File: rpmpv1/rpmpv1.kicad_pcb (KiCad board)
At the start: 2 copper layers, 102.7 x 65.3 mm, 7 parts, among them J1 RPi_GPIO, P1 CONN_02X25, U1 74LS245, U2 74LS245, U3 74LS245, U4 74LS245, U5 74LS245

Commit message: update board for RPMP
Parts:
- added REF**: 1pin, Connectors:1pin, F.Cu at (128.5, 58.3)
- added REF**: 1pin, Connectors:1pin, F.Cu at (186.5, 58.3)
- U2: moved to B.Cu
- U4, U5: moved to F.Cu
- moved J1 49.9 mm to (181.6, 59.6), turned to 90 degrees
- moved U1 20.5 mm to (175.5, 80.0), turned to 270 degrees
- moved U4 20.4 mm to (157.8, 80.0), turned to 270 degrees
- moved U3 20.3 mm to (139.4, 80.0)
- moved U5 8.92 mm to (140.7, 80.0)
- moved U2 4.47 mm to (157.8, 80.0), turned to 270 degrees
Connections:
- U1 pad 16: /INT -> /BUSDIR
- U1 pad 17: /WAIT -> /INT
- U1 pad 18: /BUSDIR -> /WAIT
- U1 pad 2: /RBUSDIR -> /RWAIT
- U1 pad 3: /RWAIT -> /RINT
- U1 pad 4: /RINT -> /RBUSDIR
- U4 pad 11: Net-(U4-Pad11) -> /RESET
- U4 pad 12: Net-(U4-Pad12) -> /WR
- U4 pad 13: /SLTSL -> /RD
- U4 pad 14: /MREQ -> /IORQ
- U4 pad 15: /IORQ -> /MREQ
- U4 pad 16: /RD -> /SLTSL
- U4 pad 17: /WR -> Net-(U4-Pad17)
- U4 pad 18: /RESET -> Net-(U4-Pad18)
- U4 pad 2: /RA13 -> Net-(U4-Pad2)
- U4 pad 3: /RA14 -> Net-(U4-Pad3)
- U4 pad 4: /RA8 -> /RA11
- U4 pad 5: /RA12 -> /RA10
- U4 pad 6: /RA10 -> /RA12
- U4 pad 7: /RA11 -> /RA8
- U4 pad 8: Net-(U4-Pad8) -> /RA14
- U4 pad 9: Net-(U4-Pad9) -> /RA13
- U5 pad 11: /A1 -> /A6
- U5 pad 12: /A0 -> /A7
- U5 pad 13: /A3 -> /A4
- U5 pad 14: /A2 -> /A5
- U5 pad 15: /A5 -> /A2
- U5 pad 16: /A4 -> /A3
- U5 pad 17: /A7 -> /A0
- U5 pad 18: /A6 -> /A1
- U5 pad 2: /RD6 -> /RD1
- U5 pad 3: /RD7 -> /RD0
- U5 pad 4: /RD4 -> /RD3
- U5 pad 5: /RD5 -> /RD2
- U5 pad 6: /RD2 -> /RD5
- U5 pad 7: /RD3 -> /RD4
- U5 pad 8: /RD0 -> /RD7
- U5 pad 9: /RD1 -> /RD6
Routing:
- net +5V: track 0.00 -> 149.6 mm, vias 0 -> 1
- net GND: track 0.00 -> 142.3 mm, vias 0 -> 13
- net /RCLK: track 0.00 -> 92.5 mm
- net /CLK: track 0.00 -> 80.2 mm, vias 0 -> 2
- net /RD4: track 0.00 -> 73.5 mm, vias 0 -> 1
- net /RWAIT: track 0.00 -> 66.4 mm
- net /RINT: track 0.00 -> 65.9 mm, vias 0 -> 1
- net /RD: track 0.00 -> 59.7 mm, vias 0 -> 1
- net /RD2: track 0.00 -> 57.1 mm, vias 0 -> 2
- net /LE_A: track 0.00 -> 56.6 mm
- net /LE_B: track 0.00 -> 53.8 mm, vias 0 -> 1
- net /RD3: track 0.00 -> 52.7 mm, vias 0 -> 1
- net /SLTSL: track 0.00 -> 52.6 mm
- net /A6: track 0.00 -> 47.7 mm, vias 0 -> 2
- net /A7: track 0.00 -> 47.3 mm, vias 0 -> 1
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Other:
- board size 102.7 x 65.3 mm -> 65.1 x 64.4 mm

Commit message: update for rpmcv1 and rpspc
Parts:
- U1: value 74LS245 -> 74LS05; footprint Housings_SOIC:SOIC-20W_7.5x12.8mm_Pitch1.27mm -> Housings_SOIC:SOIC-14_3.9x8.7mm_Pitch1.27mm
- moved U1 0.75 mm to (175.0, 79.4), turned to 90 degrees
- renumbered REF** to REF1
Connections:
- U1 pad 1: GND -> /RWAIT
- U1 pad 10: GND -> (no net)
- U1 pad 11: Net-(U1-Pad11) -> (no net)
- U1 pad 12: Net-(U1-Pad12) -> (no net)
- U1 pad 13: Net-(U1-Pad13) -> (no net)
- U1 pad 14: Net-(U1-Pad14) -> +5V
- U1 pad 2: /RWAIT -> /WAIT
- U1 pad 4: /RBUSDIR -> /INT
- U1 pad 5: /CLK -> /RBUSDIR
- U1 pad 6: Net-(U1-Pad6) -> /BUSDIR
- U1 pad 7: Net-(U1-Pad7) -> GND
- U1 pad 8: Net-(U1-Pad8) -> /RCLK
- U1 pad 9: Net-(U1-Pad9) -> /CLK
- U2 pad 1: +5V -> GND
- U3 pad 1: /RD -> /WR
- U4 pad 1: +5V -> GND
- U5 pad 1: +5V -> GND
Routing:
- net GND: track 142.3 -> 0.00 mm, vias 13 -> 0
- net /RCLK: track 92.5 -> 56.6 mm
- net +5V: track 149.6 -> 120.6 mm, vias 1 -> 3
- net /RD: track 59.7 -> 32.6 mm, vias 1 -> 0
- net /WR: track 33.3 -> 58.6 mm, vias 1 -> 2
- net /RA8: track 22.5 -> 45.0 mm, vias 1 -> 0
- net /RWAIT: track 66.4 -> 44.8 mm
- net /RD1: track 42.4 -> 23.6 mm, vias 0 -> 1
- net /RA10: track 19.5 -> 36.8 mm, vias 1 -> 0
- net /RD5: track 37.0 -> 21.0 mm, vias 0 -> 1
- net /RD6: track 38.1 -> 23.5 mm, vias 0 -> 1
- net /RINT: track 65.9 -> 51.7 mm, vias 1 -> 0
- net /RA12: track 38.4 -> 25.9 mm
- net /RD0: track 36.0 -> 23.7 mm, vias 0 -> 1
- net /RA13: track 34.2 -> 22.6 mm
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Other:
- outline, holes or cut-outs redrawn

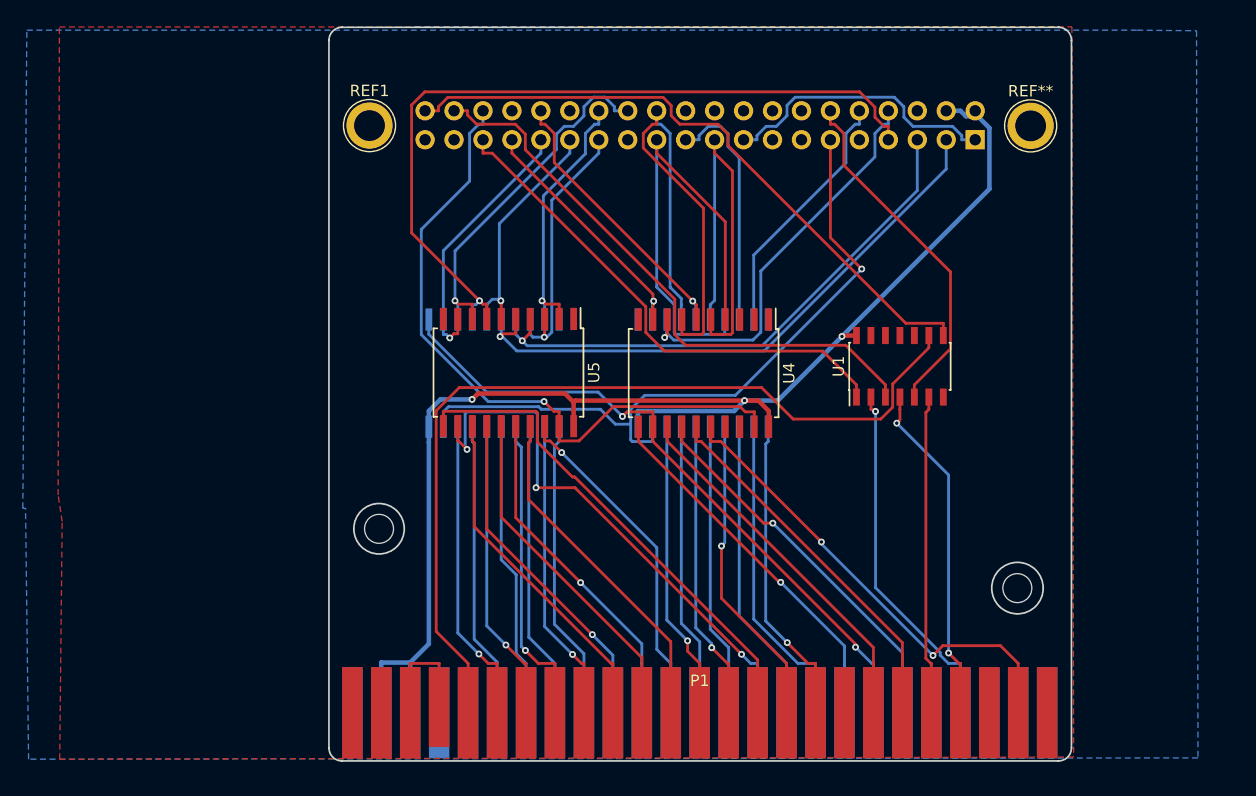
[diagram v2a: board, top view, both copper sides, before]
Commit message: improvement for RPMP feature
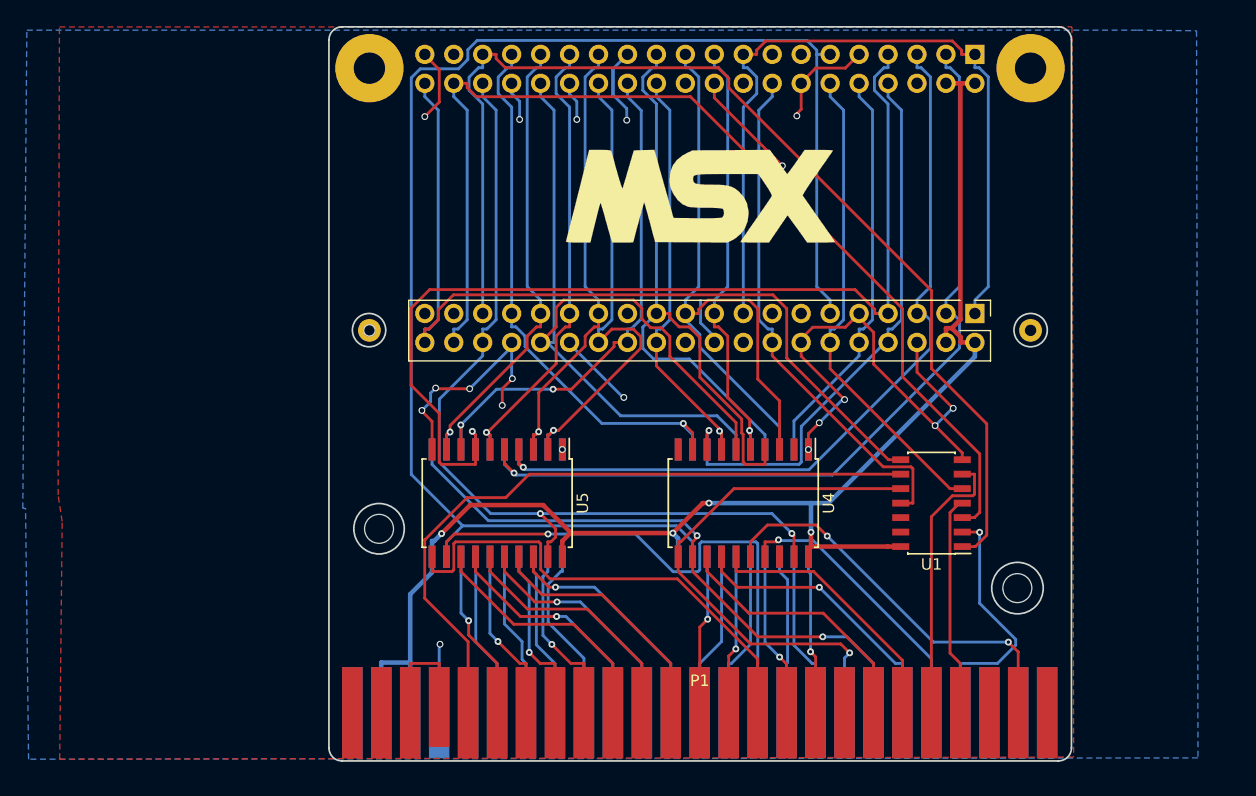
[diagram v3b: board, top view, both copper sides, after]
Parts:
- removed the REF** at (186.5, 58.3)
- removed REF1: 1pin, Connectors:1pin
- added G***: LOGO, MSX:msx-logo, F.Cu at (157.5, 64.5)
- added J2: RPi_GPIO, Socket_Strips:Socket_Strip_Straight_2x20_Pitch2.54mm, B.Cu at (181.6, 52.1)
- added REF**: Raspberry_Pi_Zero, MSX:Raspberry_Pi_Zero_Layout, F.Cu at (190.0, 49.8)
- J1: footprint Pin_Headers:Pin_Header_Straight_2x20_Pitch2.54mm -> Socket_Strips:Socket_Strip_Straight_2x20_Pitch2.54mm
- moved J1 15.2 mm to (181.6, 74.8)
- moved U1 12.3 mm to (177.8, 91.4), turned to 180 degrees
- moved U2 11.9 mm to (161.3, 91.4)
- moved U4 11.9 mm to (161.3, 91.4)
- moved U5 11.5 mm to (139.7, 91.4)
- moved U3 11.4 mm to (139.7, 91.4)
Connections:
- J1 pad 16: Net-(J1-Pad16) -> /RRESET
- P1 pad 9: Net-(P1-Pad9) -> /M1
- U1 pad 10: (no net) -> /RESET
- U1 pad 11: (no net) -> /RRESET
- U4 pad 17: Net-(U4-Pad17) -> /M1
- U4 pad 3: Net-(U4-Pad3) -> /RA9
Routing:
- net GND: track 0.00 -> 124.0 mm, vias 0 -> 19
- net /LE_B: track 62.3 -> 129.1 mm, vias 1 -> 0
- net /RWAIT: track 44.8 -> 98.6 mm
- net /RA12: track 25.9 -> 73.7 mm, vias 1 -> 0
- net /RRESET: track 0.00 -> 45.6 mm
- net +3V3: track 24.9 -> 69.6 mm
- net /RINT: track 51.7 -> 94.1 mm
- net /RA9: track 21.4 -> 59.8 mm
- net /RA13: track 22.6 -> 49.5 mm
- net /M1: track 0.00 -> 25.0 mm, vias 0 -> 1
- net /RD2: track 53.1 -> 76.7 mm
- net /RD3: track 49.3 -> 71.9 mm
- net /RA11: track 41.6 -> 63.3 mm
- net /RD4: track 69.0 -> 90.1 mm
- net /RCLK: track 56.6 -> 77.1 mm
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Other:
- outline, holes or cut-outs redrawn

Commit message: minor update for rpspc, rpmcv4, rpmpv1
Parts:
- removed the REF** at (190.0, 49.8)
- added C1: 33n, Capacitors_SMD:C_0805_HandSoldering, B.Cu at (129.5, 63.5)
- added C2: 10u, Capacitors_SMD:C_0805_HandSoldering, B.Cu at (129.5, 66.0)
- added R1: 270R, Resistors_SMD:R_0805_HandSoldering, B.Cu at (129.5, 61.0)
- added R2: 150R, Resistors_SMD:R_0805_HandSoldering, B.Cu at (129.5, 68.6)
- added REF**: Raspberry_Pi_Zero, 8BIT:Raspberry_Pi_Zero_Layout, F.Cu at (125.0, 79.7)
- moved J1 0.14 mm to (181.7, 74.9)
- moved J2 0.14 mm to (181.7, 51.9)
- renumbered P1 to ?
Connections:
- ? pad 49: Net-(P1-Pad49) -> /SOUNDIN
- J1 pad 12: /RBUSDIR -> /BCK
- J1 pad 15: Net-(J1-Pad15) -> /RBUSDIR
- J1 pad 18: Net-(J1-Pad18) -> /RWAIT
- J1 pad 22: Net-(J1-Pad22) -> /RCLK
- J1 pad 35: /RWAIT -> /LRCK
- J1 pad 40: /RCLK -> /DOUT
- J2 pad 12: /RBUSDIR -> /BCK
- J2 pad 15: Net-(J2-Pad15) -> /RBUSDIR
- J2 pad 18: Net-(J2-Pad18) -> /RWAIT
- J2 pad 22: Net-(J2-Pad22) -> /RCLK
- J2 pad 35: /RWAIT -> /LRCK
- J2 pad 40: /RCLK -> /DOUT
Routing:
- net /SOUNDIN: track 0.00 -> 45.7 mm
- net /LRCK: track 0.00 -> 38.4 mm
- net /RWAIT: track 98.6 -> 62.4 mm
- net /RCLK: track 77.1 -> 49.8 mm
- net /RA12: track 73.7 -> 49.7 mm, vias 0 -> 1
- net /DOUT: track 0.00 -> 24.0 mm
- net /BCK: track 0.00 -> 24.0 mm
- net /RA11: track 63.3 -> 42.2 mm, vias 0 -> 1
- net /RA8: track 37.4 -> 55.9 mm, vias 1 -> 0
- net /RD6: track 41.2 -> 59.6 mm, vias 1 -> 0
- net /RD4: track 90.1 -> 108.0 mm
- net /RINT: track 94.1 -> 76.6 mm
- net /RA9: track 59.8 -> 42.8 mm, vias 0 -> 1
- net /RBUSDIR: track 42.2 -> 50.5 mm
- net /A7: track 47.6 -> 39.3 mm
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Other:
- board text added: "2018.01.19"
- board text added: "5V"
- board text added: "74LS05"
- board text added: "74LS245"
- board text added: "ADDRESS"
- board text added: "BD"
- board text added: "CLK"
- board text added: "CS12"
- board text added: "DATA"
- board text added: "GND"
- board text added: "INT"
- board text added: "IQ"
- board text added: "M1"
- board text added: "MQ"
- board text added: "RD"
- board text added: "RST"
- board text added: "Rraspberry Pi extension Ver. 0.5"
- board text added: "SL"
- board text added: "WAIT"
- board text added: "WR"
- board text added: "meeso.kim@gmail.com"

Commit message: clean up for all works
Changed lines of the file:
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@@
     (links 149)
     (no_connects 5)
-    (area 98.0821 30.388775 228.708296 115.286853)
+    (area 124.867599 49.581999 190.155901 114.133701)
     (thickness 1.6)
     (drawings 53)
@@
     (mod_text_size 1 1)
     (mod_text_width 0.15)
-    (pad_size 1.7 1.7)
-    (pad_drill 0.9)
+    (pad_size 4.5 4.5)
+    (pad_drill 4.5)
     (pad_to_mask_clearance 0.2)
     (aux_axis_origin 0 0)
@@
     (fp_circle (center -26.873455 -12.985388) (end -25.523455 -12.985388) (layer Dwgs.User) (width 0.1))
     (fp_arc (start 32.846865 7.356852) (end 32.846865 8.356852) (angle -90) (layer Dwgs.User) (width 0.1))
-    (pad "" np_thru_hole circle (at 29.12364 -7.78256) (size 2.54 2.54) (drill 2.54) (layers *.Cu *.Mask F.SilkS)
+    (pad "" np_thru_hole circle (at 29.12364 -7.78256) (size 4.5 4.5) (drill 4.5) (layers *.Cu *.Mask F.SilkS)
       (clearance 1))
     (pad 1 connect rect (at 31.73984 3.14744) (size 1.8 8) (layers B.Cu B.Mask)
@@
     (pad 50 connect rect (at -29.22016 3.14744) (size 1.8 8) (layers F.Cu F.Mask)
       (net 70 "Net-(P1-Pad50)"))
-    (pad "" np_thru_hole circle (at -26.87574 -12.98448) (size 2.54 2.54) (drill 2.54) (layers *.Cu *.Mask F.SilkS)
+    (pad "" np_thru_hole circle (at -26.87574 -12.98448) (size 4.5 4.5) (drill 4.5) (layers *.Cu *.Mask F.SilkS)
       (clearance 1))
   )
